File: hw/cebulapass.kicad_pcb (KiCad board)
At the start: 2 copper layers, 85.6 x 54 mm, 2 parts, among them U1 NRF24L01_Breakout, U2 STM32F070CBTx

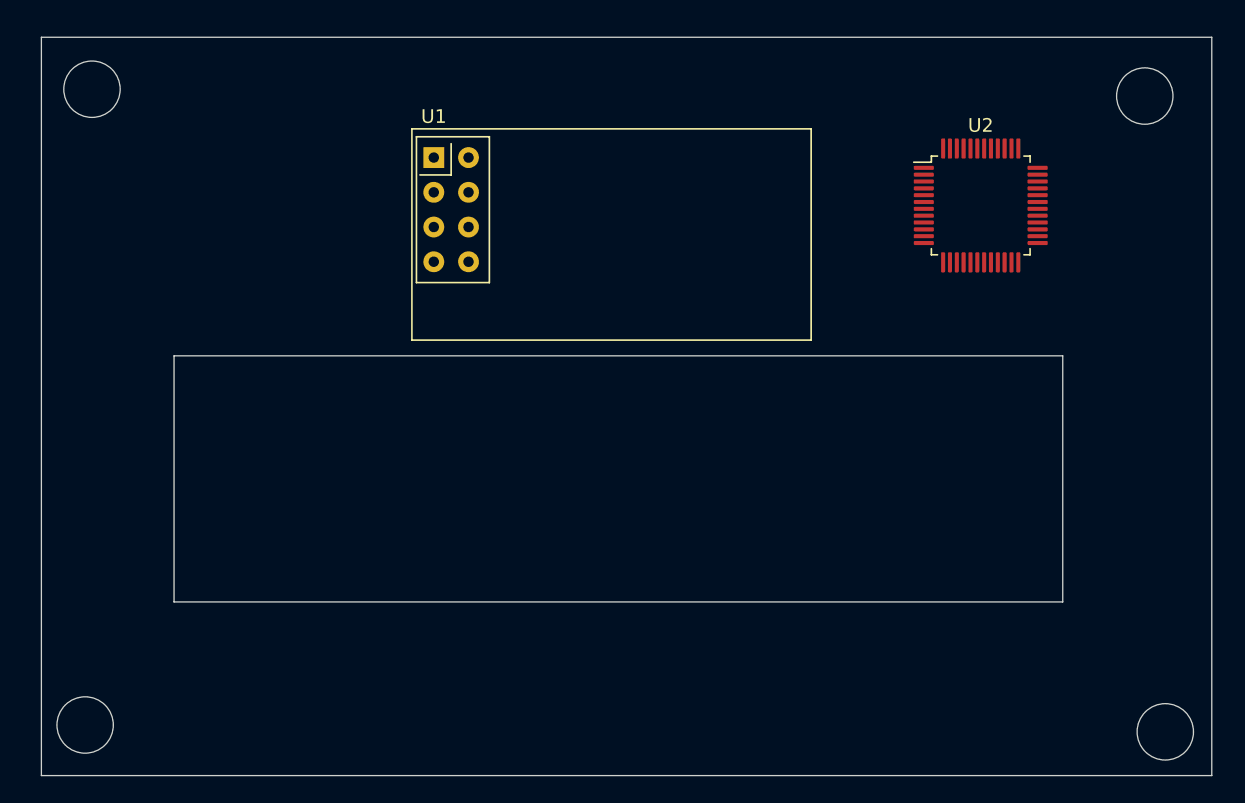
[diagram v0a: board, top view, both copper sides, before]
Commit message: Adding nRF24 and USB-on-PCB
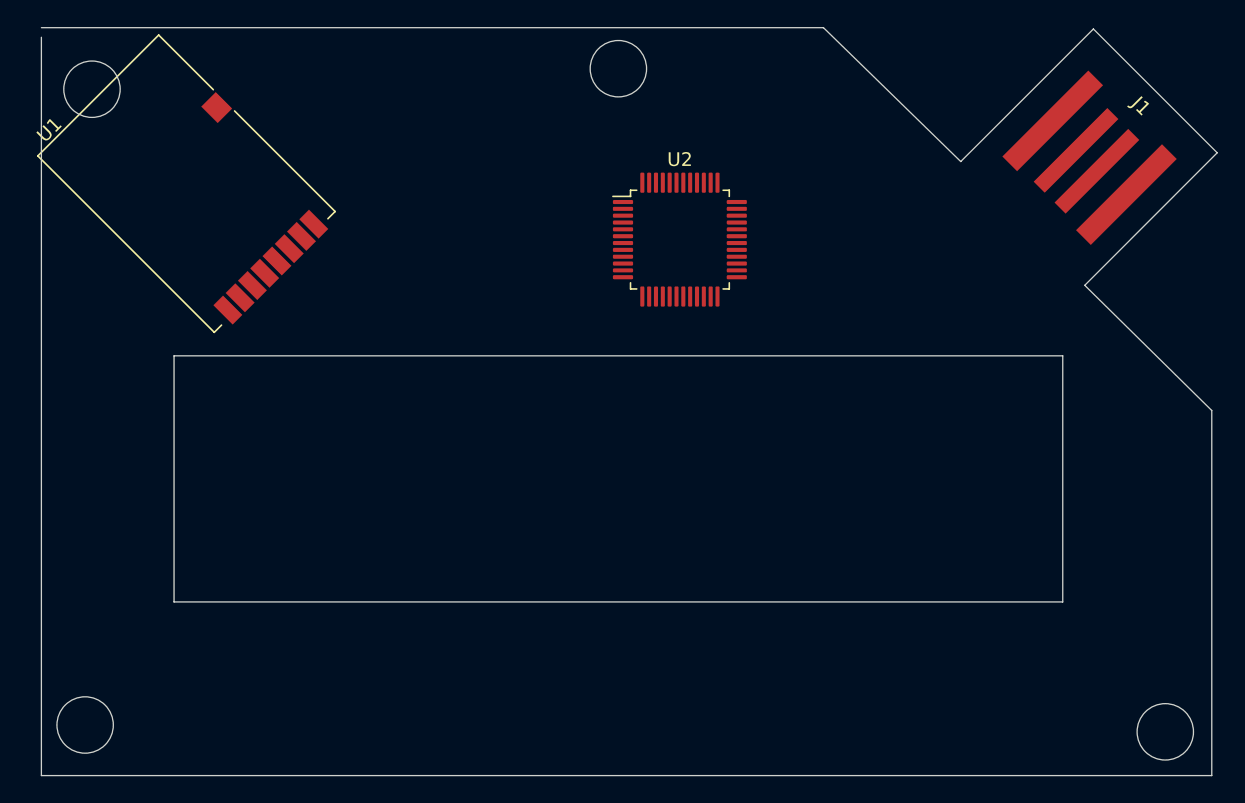
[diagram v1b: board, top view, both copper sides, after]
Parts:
- added J1: USB_A, Connector_USB:USB_A_Pads_On_PCB, F.Cu at (137.1, 61.4)
- U1: value NRF24L01_Breakout -> NRF24L01_Breakout_Smd; footprint RF_Module:nRF24L01_Breakout -> RF_Module:nRF24L01_Breakout_Smd
- moved U2 22.1 mm to (112.0, 62.5)
- moved U1 18.1 mm to (76.0, 58.5), turned to 45 degrees
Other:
- board size 85.6 x 54 mm -> 86 x 54.7 mm
